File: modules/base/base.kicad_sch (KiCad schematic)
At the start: 74 parts, among them J1 LineOut, J2 Ground, J4 Ground, J5 USB_C_Receptacle_PowerOnly_6P, J6 HeadphoneOut, SW1 K2-1808SN-A4SW-01, U2 MCP6002-xSN, U3 MCP6002-xSN, U4 MCP6002-xSN, U5 AP2112K-3.3

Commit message: base: line-out default gain 330k->680k for R18/R19 (+6.28 dB); record remaining loud-jumper/normalling work as pending in CHANGELOG
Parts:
- R18, R19: value 330k -> 680k
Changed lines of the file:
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@@
 			)
 		)
-		(property "Value" "330k"
+		(property "Value" "680k"
 			(at 97.79 381 90)
 			(effects
@@
 			)
 		)
-		(property "Value" "330k"
+		(property "Value" "680k"
 			(at 97.79 336.55 90)
 			(effects

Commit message: base: 1.3.4 - remove the leaky R25 IN_L-IN_R bridge, add the unilateral 2M R52 mono normal (J19 solder-jumper link), move R24's DC return to the 1.65V +2.5V node (R5 1M->2M); record the Phase-2 loud-gain shunt as deferred
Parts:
- removed R25: 10k, Resistor_SMD:R_0402_1005Metric, symbol Device:R
- added J19: SolderJumper_2_Bridged, Jumper:SolderJumper-2_P1.3mm_Bridged_Pad1.0x1.5mm, symbol Connector_Generic:Conn_01x02
- added R52: 2M, Resistor_SMD:R_0402_1005Metric, symbol Device:R
- R24: value 10k -> 2M; LCSC C25744 -> C11512; MPN 0402WGF1002TCE -> 0402WGF2004TCE
- R5: value 1M -> 2M; LCSC C26083 -> C11512; MPN 0402WGF1004TCE -> 0402WGF2004TCE
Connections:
- net +2.5V: now also R24.2
- net BUFF_IN_R: now also R52.2
- net GND: no longer R24.2
- net IN_L: now also J19.1 (Pin_1)
- new net NORM_R: J19.2 (Pin_2), R52.1

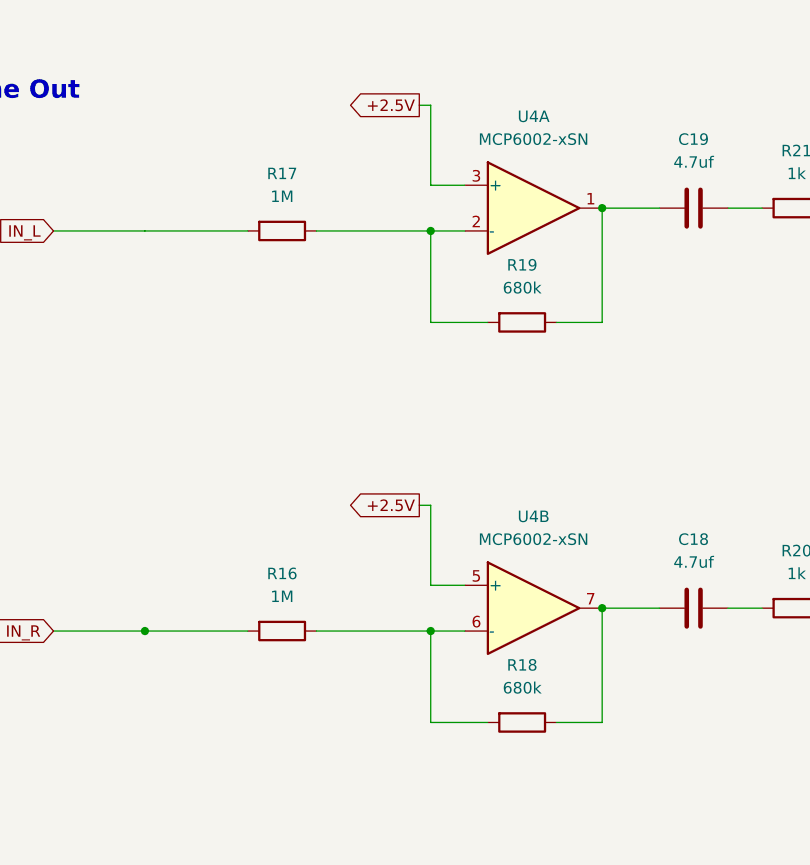
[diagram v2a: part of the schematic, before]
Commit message: base: 1.3.5 - line-out loud-gain option: 1M series R53/R54 + shunt solder jumper J20/J21 per channel (bridged as shipped = 680k default / +6.28 dB, cut = 1.68M / +14.14 dB vs the 330k board); schematic re-wired with the LFB_A/LFB_B and RFB_A/RFB_B nodes
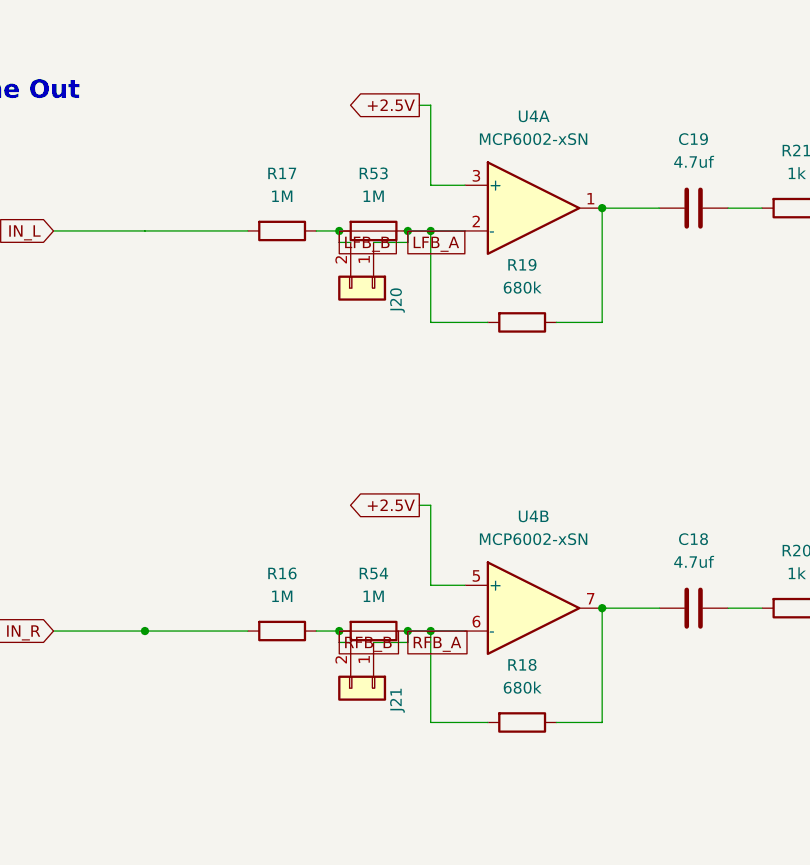
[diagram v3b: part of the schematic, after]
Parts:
- added J20, J21: SolderJumper_2_Bridged, Jumper:SolderJumper-2_P1.3mm_Bridged_Pad1.0x1.5mm, symbol Connector_Generic:Conn_01x02
- added R53, R54: 1M, Resistor_SMD:R_0402_1005Metric, symbol Device:R
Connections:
- net RFB_A: now reaches R18.2, U4.6 (-)
- net RFB_A: now also J21.1 (Pin_1), R54.1; no longer R16.1
- net LFB_A: now reaches R19.2, U4.2 (-)
- net LFB_A: now also J20.1 (Pin_1), R53.1; no longer R17.1
- new net LFB_B: J20.2 (Pin_2), R17.1, R53.2
- new net RFB_B: J21.2 (Pin_2), R16.1, R54.2

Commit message: base: correct the stale R18/R19 part numbers (330 k part under a 680 k value)
The 1.3.3 value change (330 k -> 680 k) touched only the Value property, so
R18/R19 kept pointing at the 330 k part: LCSC C23137 / MPN 0603WAF3303T5E =
UNI-ROYAL 0603WAF3303T5E, 330 k 0603. Corrected in both base.kicad_sch and
base.kicad_pcb (LCSC + MPN, one property each per reference); no other field,
no geometry, no net, no copper.

* New part: UNI-ROYAL 0603WAF6803T5E / LCSC C25822 - RES 680 kOhm +-1% 100 mW
  0603, 75 V, +-100 ppm/C. Verified on the LCSC product page and on the JLCPCB
  parts page (both in stock and JLCPCB-assembled: LCSC ~1.19 M available,
  $0.0011-0.0017 @1k+; JLCPCB part # C25822). Same manufacturer, series,
  package and tolerance as the part it replaces, so no other field changes.
* Value (680k), Manufacturer (UNI-ROYAL), Footprint
  (Resistor_SMD:R_0603_1608Metric) and Datasheet ("~", the chip-resistor
  convention already used by every other resistor here) are unchanged.
* Audited every part whose value changed on this branch (merge-base 1b9d03c):
  R5 1 M -> 2 M and R24 10 k -> 2 M both carry C11512 / 0402WGF2004TCE, and the
  new R52 (2 M), R53/R54 (1 M, C26083 / 0402WGF1004TCE) and J19/J20/J21 (solder
  jumpers: no LCSC/MPN by design, in_bom no, excluded from BOM and position
  files) are all already consistent. R18/R19 were the only stale rows.
* Verification: `kicad-cli sch erc` 11 findings, identical set before/after;
  `kicad-cli pcb drc --schematic-parity` 82 warnings / 0 unconnected / 145
  schematic-parity, identical set before/after (no new findings); the exported
  BOM diff is exactly one line, 680k/C23137 -> 680k/C25822.
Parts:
- R18, R19: LCSC C23137 -> C25822; MPN 0603WAF3303T5E -> 0603WAF6803T5E
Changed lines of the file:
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@@
 			)
 		)
-		(property "LCSC" "C23137"
-			(at 0 0 0)
-			(effects
-				(font
-					(size 1.27 1.27)
-				)
-				(hide yes)
-			)
-		)
-		(property "MPN" "0603WAF3303T5E"
+		(property "LCSC" "C25822"
+			(at 0 0 0)
+			(effects
+				(font
+					(size 1.27 1.27)
+				)
+				(hide yes)
+			)
+		)
+		(property "MPN" "0603WAF6803T5E"
 			(at 0 0 0)
 			(effects
@@
 			)
 		)
-		(property "LCSC" "C23137"
-			(at 0 0 0)
-			(effects
-				(font
-					(size 1.27 1.27)
-				)
-				(hide yes)
-			)
-		)
-		(property "MPN" "0603WAF3303T5E"
-			(at 0 0 0)
-			(effects
+		(property "LCSC" "C25822"
+			(at 0 0 0)
+			(effects
+				(font
+					(size 1.27 1.27)
+				)
+				(hide yes)
+			)
+		)
+		(property "MPN" "0603WAF6803T5E"
+			(at 0 0 0)
+			(effects

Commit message: base: 1.3.6 Phase A - remove the passive mono normal (R52+J19), restore the symmetric stereo input path
- delete R52 + J19 and the NORM_R net (schematic, plus the PCB copper that only fed them: the
  IN_L stub to J19.1, R52's F.Cu stub, the BUFF_IN_R B.Cu trunk+jog and the via at
  (233.700,88.500)); BUFF_IN_R keeps its U2.6/U2.7 -> RV1.3 path, nothing is left dangling
- R5 2M pin 1 moves from BUFF_IN_L to the 1.65V node +2.5V, so R5 (right) and R24 (left) are
  identical per-channel bias returns: 2M||1M = 667k input impedance and -680k/1M = -0.68 =
  -3.35 dB on both channels (0.000 dB L/R difference), no DC current in R17/R16 and both amp
  outputs at 1.65V; 2M keeps the already-sourced C11512 part and does not load the 500R bias
  source (a 2M return also does not shift the node off 1.65V)
- PCB: R5 is not moved; R5.1 -> 1 F.Cu stub -> 1 via -> 2 B.Cu segments landing on the existing
  +2.5V horizontal at y=90.062 (an all-F.Cu route is impossible: the IN_L trace walls the pocket)
- correct a latent net-code bug: the existing (241.929,64.643)-(240.411,64.643) +2.5V return
  segment was still stored as net 1 (GND); now net 18 (+2.5V). No geometry change
- verification: sch erc == baseline (11 findings, identical kinds); pcb drc --schematic-parity
  == 0 errors / 0 unconnected / 145 parity items (== baseline); 80 violations = 71
  lib_footprint_mismatch (baseline 73 minus the two removed footprints) + the baseline's 5
  silk_overlap and 4 silk_over_copper, i.e. no new item. Netlist proof: 1.3.5 has
  BUFF_IN_L -R5- IN_R and BUFF_IN_R -R52- NORM_R -J19- IN_L; this revision has no passive path
  between the left and right signal chains (supply/GND excluded)
- headphone block and the loud-gain parts byte-identical (U3, R6/R7, RV1/RV2, C3/C7-C13,
  R8/R9/R10/R12, J1, J6, C18/C19, R20/R21, R53/R54+J20/J21, R16/R17/R18/R19, U2/U4, R14/R15)
- board diff 791+/1266-: 1503 of those lines are the re-poured B.Cu GND polygon (only 1 of the
  49 filled polygons changed)
- VERSION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
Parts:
- removed J19: SolderJumper_2_Bridged, Jumper:SolderJumper-2_P1.3mm_Bridged_Pad1.0x1.5mm, symbol Connector_Generic:Conn_01x02
- removed R52: 2M, Resistor_SMD:R_0402_1005Metric, symbol Device:R
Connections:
- net +2.5V: now also R5.1
- net BUFF_IN_L: no longer R5.1

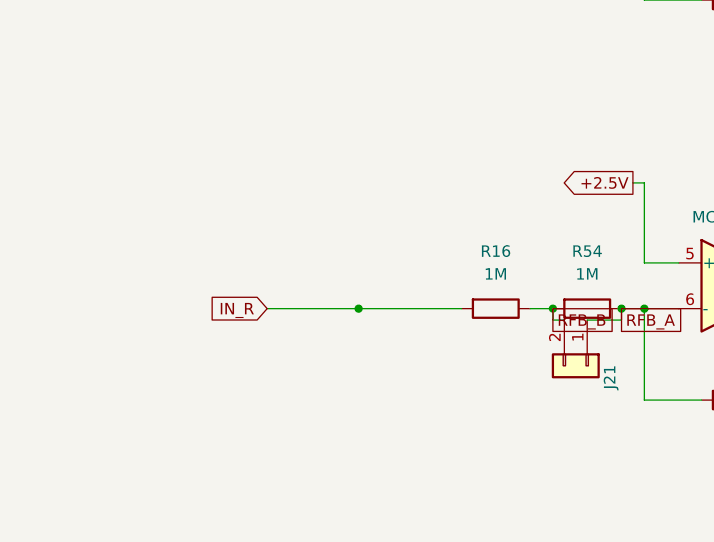
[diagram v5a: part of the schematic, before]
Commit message: base: 1.3.6 Phase B - mono mode as a selector jumper at the right line-amp input (J22), right input discarded
- J22 = Jumper:SolderJumper-3_P1.3mm_Bridged12_Pad1.0x1.5mm at (250.317,66.5), symbol
  Connector_Generic:Conn_01x03 with Value SolderJumper_3_Bridged12 (in_bom no) and
  net_tie_pad_groups "1, 2": pad 1 = IN_R, pad 2 = RIN_SEL (new net) = R16's input pin,
  pad 3 = BUFF_IN_L
- as shipped (pads 1-2 bridged) the right line-amp input is its own channel input IN_R: pure
  stereo, no passive path between the left and right chains
- mono (cut the 1-2 bridge, bridge 2-3) drives the right line amp from the buffered LEFT signal
  while IN_R is reduced to its 2M bias return R5, so the right input reaches no line output
- level: unity-gain buffer + R16 = R17 = 1M into R18 = R19 = 680k gives -0.68 = -3.35 dB on both
  channels in both positions (0.00 dB L/R; loud state -(680k+1M)/1M = -4.51 dB on both too), so no
  series resistor is needed; DC: RIN_SEL sits at 1.65V in both positions (no DC step, no offset
  through R16)
- PCB: the old IN_R run into R16.2 is replaced by three F.Cu links (J22.2 -> R16.2; J22.1 -> IN_R,
  with the old 45-degree jog removed so nothing dangles; J22.3 -> BUFF_IN_L through x = 252.9).
  All new copper is F.Cu only, so this phase re-poured no zone
- verification: sch erc == baseline (11 findings, identical kinds); pcb drc --schematic-parity ==
  0 errors / 0 unconnected / 146 parity items (145 baseline + J22's field comparison, same class);
  81 violations = 72 lib_footprint_mismatch + the baseline's 5 silk_overlap and 4
  silk_over_copper - no new violation class, no new silkscreen item
- netlist proof: stereo = no passive path between the chains; mono = the only path is the intended
  BUFF_IN_L -J22- RIN_SEL -R16- RFB_B, with IN_R left with just its 2M bias return
- headphone block and loud-gain parts byte-identical (U3, R6/R7, RV1/RV2, C3/C7-C13, R8/R9/R10/R12,
  J1, J6, C18/C19, R20/R21, R53/R54+J20/J21): mono is confined to the line out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
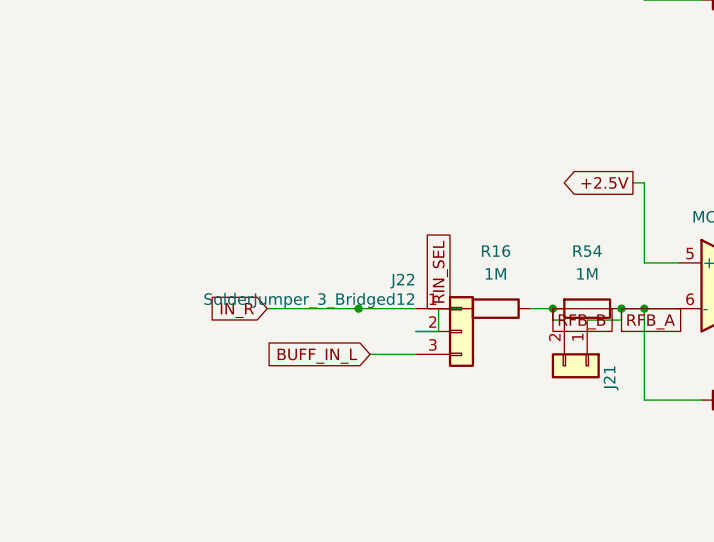
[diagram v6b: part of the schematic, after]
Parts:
- added J22: SolderJumper_3_Bridged12, Jumper:SolderJumper-3_P1.3mm_Bridged12_Pad1.0x1.5mm, symbol Connector_Generic:Conn_01x03
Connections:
- net BUFF_IN_L: now also J22.3 (Pin_3)
- net IN_R: now also J22.1 (Pin_1); no longer R16.2
- new net RIN_SEL: J22.2 (Pin_2), R16.2
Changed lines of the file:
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@@
 	(wire
 		(pts
-			(xy 55.88 374.65) (xy 67.31 374.65)
+			(xy 55.88 374.65) (xy 62.23 374.65)
 		)
 		(stroke
@@
 	(wire
 		(pts
+			(xy 62.23 377.19) (xy 64.77 377.19)
+		)
+		(stroke
+			(width 0)
+			(type default)
+		)
+	)
+	(wire
+		(pts
+			(xy 64.77 377.19) (xy 64.77 374.65)
+		)
+		(stroke
+			(width 0)
+			(type default)
+		)
+	)
+	(wire
+		(pts
+			(xy 64.77 374.65) (xy 67.31 374.65)
+		)
+		(stroke
+			(width 0)
+			(type default)
+		)
+	)
+	(wire
+		(pts
+			(xy 57.15 379.73) (xy 62.23 379.73)
+		)
+		(stroke
+			(width 0)
+			(type default)
+		)
+	)
+	(global_label "RIN_SEL" (shape passive) (at 64.77 374.65 90) (fields_autoplaced yes)
+		(effects
+			(font
+				(size 1.27 1.27)
+			)
+			(justify left)
+		)
+		(property "Intersheetrefs" "${INTERSHEET_REFS}"
+			(at 64.77 373.0 90)
+			(effects
+				(font
+					(size 1.27 1.27)
+				)
+				(justify left)
+				(hide yes)
+			)
+		)
+	)
+	(global_label "BUFF_IN_L" (shape input) (at 57.15 379.73 180) (fields_autoplaced yes)
+		(effects
+			(font
+				(size 1.27 1.27)
+			)
+			(justify right)
+		)
+		(property "Intersheetrefs" "${INTERSHEET_REFS}"
+			(at 57.15 386.53 180)
+			(effects
+				(font
+					(size 1.27 1.27)
+				)
+				(justify right)
+				(hide yes)
+			)
+		)
+	)
+	(wire
+		(pts
 			(xy 132.08 327.66) (xy 138.43 327.66)
 		)
@@
 					(unit 1)
 				)
+			)
+		)
+	)
+	(symbol
+		(lib_id "Connector_Generic:Conn_01x03")
+		(at 67.31 377.19 0)
+		(unit 1)
+		(exclude_from_sim no)
+		(in_bom no)
+		(on_board yes)
+		(dnp no)
+		(property "Reference" "J22"
+			(at 62.23 371.475 0)
+			(effects
+				(font
+					(size 1.27 1.27)
+				)
+				(justify right)
+			)
+		)
+		(property "Value" "SolderJumper_3_Bridged12"
+			(at 62.23 373.6349 0)
+			(effects
+				(font
+					(size 1.27 1.27)
+				)
+				(justify right)
+			)
+		)
+		(property "Footprint" "Jumper:SolderJumper-3_P1.3mm_Bridged12_Pad1.0x1.5mm"
+			(at 67.31 377.19 0)
+			(effects
+				(font
+					(size 1.27 1.27)
+				)
+				(hide yes)
+			)
+		)
+		(property "Datasheet" ""
+			(at 67.31 377.19 0)
+			(effects
+				(font
+					(size 1.27 1.27)
+				)
+				(hide yes)
+			)
+		)
+		(property "Description" "Line-out stereo/mono selector (3-pad solder jumper, pads 1-2 bridged as shipped): pin1 = IN_R (stereo), pin2 = the right line amplifier input (R16), pin3 = BUFF_IN_L (mono). Cut the 1-2 bridge and bridge 2-3 for mono; in mono the right input IN_R no longer reaches the right line output."
+			(at 67.31 377.19 0)
+			(effects
+				(font
+					(size 1.27 1.27)
+				)
+				(hide yes)
+			)
+		)
+		(property "LCSC" ""
+			(at 67.31 377.19 0)
+			(effects
+				(font
+					(size 1.27 1.27)
+				)
+				(hide yes)
+			)
+		)
+		(property "MPN" ""
+			(at 67.31 377.19 0)
+			(effects
+				(font
+					(size 1.27 1.27)
+				)
+				(hide yes)
+			)
+		)
+		(pin "1"
+		)
+		(pin "2"
+		)
+		(pin "3"
+		)
+		(instances
+			(project "base"
+				(path "/b63493d3-5f6d-47e3-845b-87e7090fc1ab"
+					(reference "J22")
+					(unit 1)
+				)

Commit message: base: 1.3.7 (WIP checkpoint) - real MONO/GAIN jumpers + mux (U18/U19, J23/J24), gain-leg wiring fix, schematic legibility pass; PCB pending
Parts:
- removed J20, J21: SolderJumper_2_Bridged, Jumper:SolderJumper-2_P1.3mm_Bridged_Pad1.0x1.5mm, symbol Connector_Generic:Conn_01x02
- removed J22: SolderJumper_3_Bridged12, Jumper:SolderJumper-3_P1.3mm_Bridged12_Pad1.0x1.5mm, symbol Connector_Generic:Conn_01x03
- added C48, C49: 100n, Capacitor_SMD:C_0402_1005Metric, symbol Device:C
- added J23, J24: PZ200-1-02-Z, Connector_PinHeader_2.00mm:PinHeader_1x02_P2.00mm_Vertical, symbol Connector_Generic:Conn_01x02
- added R55, R56: 100k, Resistor_SMD:R_0402_1005Metric, symbol Device:R
- added U18, U19: TS5A23157DGS, Package_SO:TSSOP-10_3x3mm_P0.5mm, symbol Analog_Switch:TS5A23157DGS
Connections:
- net +3.3V: now also C48.1, C49.1, J23.1 (Pin_1), J24.1 (Pin_1), U18.8 (VCC), U19.8 (VCC)
- net BUFF_IN_L: now also U18.2
- net GND: now also C48.2, C49.2, R55.2, R56.2, U18.3 (GND), U18.4, U18.6, U18.7, U19.3 (GND)
- net IN_R: now also U18.9
- net LFB_A: now also U19.9; no longer U4.2 (-)
- net LFB_B: now also U4.2 (-), U19.10
- net RFB_A: now also U19.7; no longer U4.6 (-)
- net RFB_B: now also U4.6 (-), U19.6
- net RIN_SEL: now also U18.10
- new net GAIN_SEL: J24.2 (Pin_2), R56.1, U19.1, U19.5
- new net MONO_SEL: J23.2 (Pin_2), R55.1, U18.1, U18.5
- no-connect marks 0 -> 2
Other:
- note added: "LINE-OUT GAIN SELECT J24 (1x02 2.00 mm header + shunt C5664) -> U19: one jumper moves BOTH channels (IN1 = IN2 = GAIN_SEL), closed loop in both states. Shunt ABSENT or LOST = SEL low (R56 100k pulldown) -> U19 IN = L -> COM-NC closed -> R53/R54 shorted -> Rf = R19/R18 = 680k -> 0.68 = -3.35 dB (the shipped default). Shunt FITTED = SEL high (+3.3 V) -> IN = H -> COM-NO open -> Rf = 680k + 1M = 1.6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"
- note added: "MONO / STEREO SELECT J23 (1x02 2.00 mm header + shunt C5664) -> U18 Shunt FITTED = SEL high (+3.3 V) -> U18 IN = H -> COM1-NO1 closed: the right LINE-OUT amplifier input is driven by BUFF_IN_L (mono) and IN_R is disconnected from it. Shunt ABSENT or LOST = SEL low (R55 100k pulldown) -> IN = L -> COM1-NC1 closed: the right amp input is driven by its own IN_R (stereo, as shipped). Left line-out an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"

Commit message: Update the base schematics
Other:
- note added: "# Mono Selector When jumper patched, output will be mono. Left In will be sent to right."
- note added: "#7db Loud Toggle."
- note removed: "BASE v1.3.0 POWER UPGRADE - see POWER.md F1/D2 protect VBUS at the USB-C input; 5V_SYS is tapped from protected VBUS (after F1, before FB1) through F2, D3 and 100uF/0.1uF bulk. 12 x per-slot 2:1 power mux (U6..U17): shunt fitted -> 5V_SYS, open/lost -> +3.3V (100k pulldown). J7..J18 sit hidden under a mated module: place them over the slot power rail, not in the ground/power gap. Protection hiera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"
- note removed: "LINE-OUT GAIN SELECT J24 (1x02 2.00 mm header + shunt C5664) -> U19: one jumper moves BOTH channels (IN1 = IN2 = GAIN_SEL), closed loop in both states. Shunt ABSENT or LOST = SEL low (R56 100k pulldown) -> U19 IN = L -> COM-NC closed -> R53/R54 shorted -> Rf = R19/R18 = 680k -> 0.68 = -3.35 dB (the shipped default). Shunt FITTED = SEL high (+3.3 V) -> IN = H -> COM-NO open -> Rf = 680k + 1M = 1.6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"
- note removed: "MONO / STEREO SELECT J23 (1x02 2.00 mm header + shunt C5664) -> U18 Shunt FITTED = SEL high (+3.3 V) -> U18 IN = H -> COM1-NO1 closed: the right LINE-OUT amplifier input is driven by BUFF_IN_L (mono) and IN_R is disconnected from it. Shunt ABSENT or LOST = SEL low (R55 100k pulldown) -> IN = L -> COM1-NC1 closed: the right amp input is driven by its own IN_R (stereo, as shipped). Left line-out an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"
- note removed: "One sheet symbol = one instance of the slot template: supply + ground socket, TPS2111A 2:1 power mux, 750R ILIM, 100k SEL pulldown, decoupling and the 1x02 rail-select header. Sheet pins VSLOT / SEL carry the per-slot rail and select nets (VSLOT_n / SEL_n) - the netlist is unchanged."
- moved on the sheet: 5V14, C10, C11, C12, C13, C18, C19, C3, C46, C47, C48, C49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
